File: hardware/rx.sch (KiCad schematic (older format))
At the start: 19 parts, among them P1 SMA, U11 SKY65404, U9 TRF37A73

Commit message: Current working version.
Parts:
- C179, C180, C42, C44, C46, C48, C49: footprint fmcw3:C_0402b -> Capacitor_SMD:C_0402_1005Metric; symbol C -> Device:C
- C35, C47, C50, C54: footprint fmcw3:C_0603b -> Capacitor_SMD:C_0603_1608Metric; symbol C -> Device:C
- FB7, FB8: symbol FILTER -> Device:Ferrite_Bead
- L1, L2: symbol INDUCTOR -> Device:L
- P1: symbol SMA -> fmcw3-rescue:SMA
- R22: symbol R -> Device:R
- U11: symbol SKY65404 -> fmcw3-rescue:SKY65404
- U9: symbol TRF37A75 -> fmcw3-rescue:TRF37A75
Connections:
- wire segments 39 -> 54

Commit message: Dropped the 3 from the end of the project name.
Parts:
- FB7, FB8: footprint fmcw3:C_0603b -> fmcw:C_0603b
- L1, L2: footprint fmcw3:C_0402b -> fmcw:C_0402b
- P1: footprint fmcw3:CONSMA003.062 -> fmcw:CONSMA003.062; symbol fmcw3-rescue:SMA -> fmcw-rescue:SMA-fmcw3-rescue
- R22: footprint fmcw3:R_0402b -> fmcw:R_0402b
- U11: footprint fmcw3:XFDFN-6 -> fmcw:XFDFN-6; symbol fmcw3-rescue:SKY65404 -> fmcw-rescue:SKY65404-fmcw3-rescue
- U9: footprint fmcw3:DFN-8-1EP_2x2mm_Pitch0.5mm -> fmcw:DFN-8-1EP_2x2mm_Pitch0.5mm; symbol fmcw3-rescue:TRF37A75 -> fmcw-rescue:TRF37A75-fmcw3-rescue

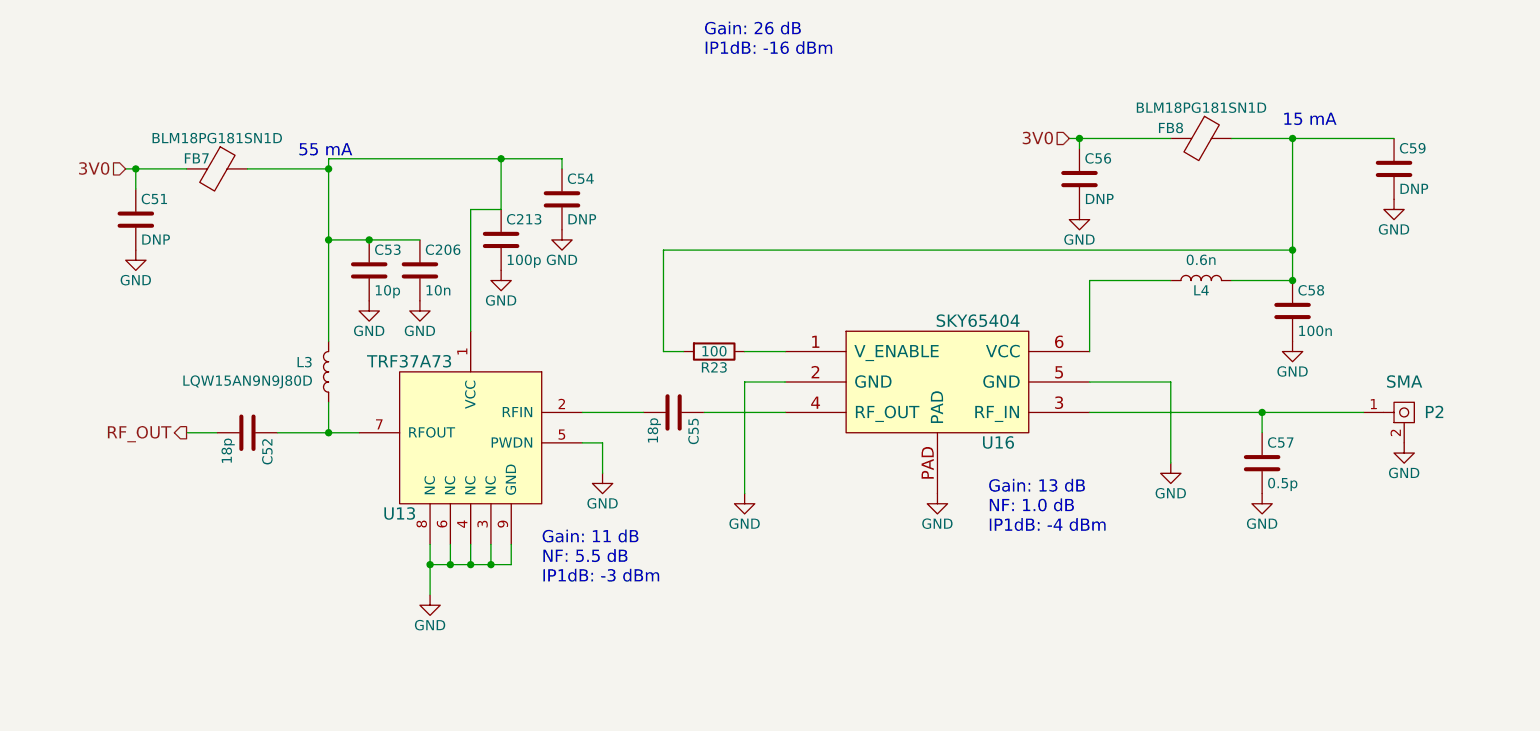
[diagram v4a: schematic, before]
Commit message: Improved top level documentation.
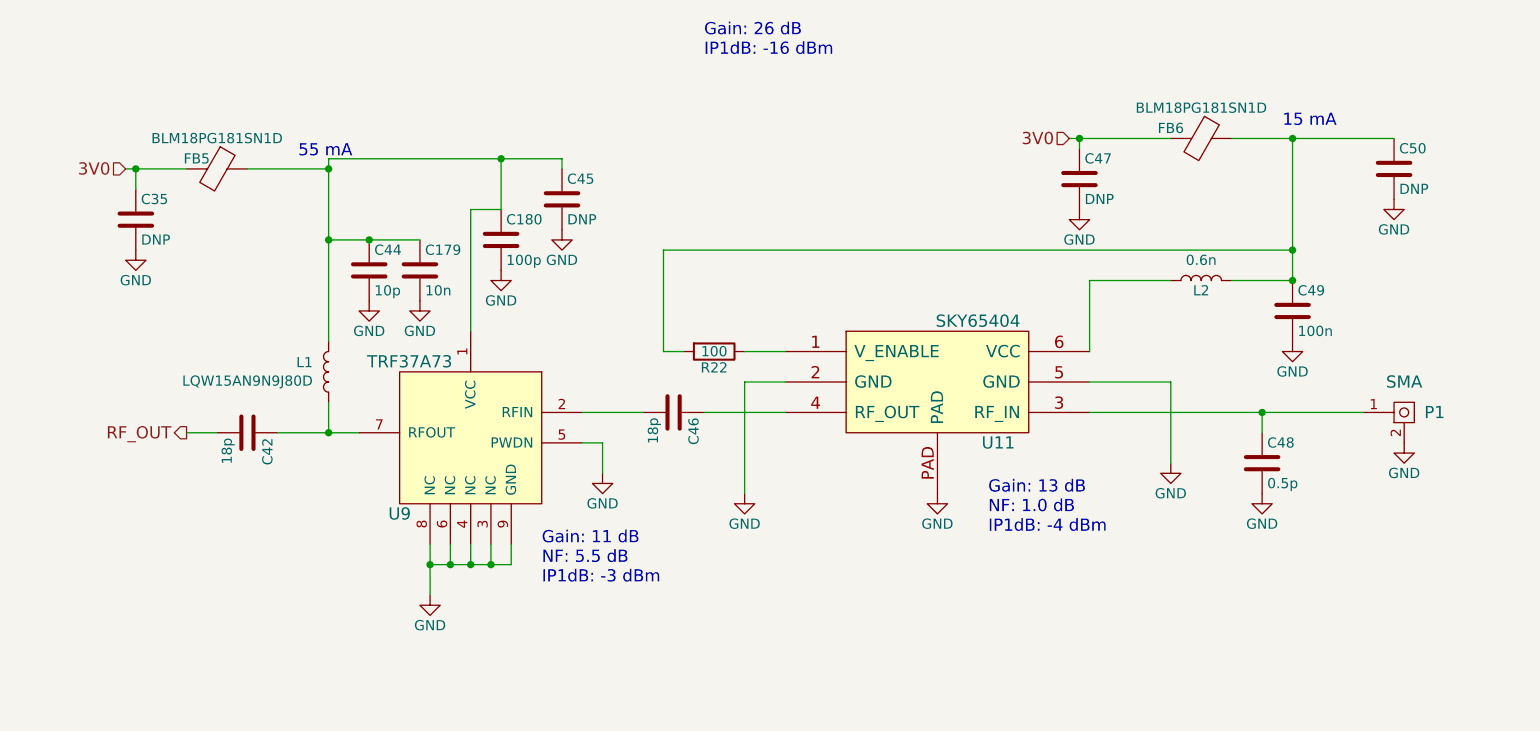
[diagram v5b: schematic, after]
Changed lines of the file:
@@
 $Descr A4 11693 8268
 encoding utf-8
-Sheet 7 10
+Sheet 6 10
 Title ""
 Date ""
@@
 AR Path="/59396B97/593BC199" Ref="U11"  Part="1"
 AR Path="/593D90BA/593BC199" Ref="U16"  Part="1"
-F 0 "U16" H 7150 3500 60  0000 C CNN
+F 0 "U11" H 7150 3500 60  0000 C CNN
 F 1 "SKY65404" H 7050 4100 60  0000 C CNN
 F 2 "fmcw:XFDFN-6" H 6750 3800 60  0001 C CNN
@@
 AR Path="/59396B97/593BC25F" Ref="#PWR0124"  Part="1"
 AR Path="/593D90BA/593BC25F" Ref="#PWR0139"  Part="1"
-F 0 "#PWR0139" H 6850 4100 50  0001 C CNN
+F 0 "#PWR0124" H 6850 4100 50  0001 C CNN
 F 1 "GND" H 6850 4200 50  0000 C CNN
 F 2 "" H 6850 4350 60  0000 C CNN
@@
 AR Path="/59396B97/593BC2B3" Ref="#PWR0125"  Part="1"
 AR Path="/593D90BA/593BC2B3" Ref="#PWR0140"  Part="1"
-F 0 "#PWR0140" H 8000 3950 50  0001 C CNN
+F 0 "#PWR0125" H 8000 3950 50  0001 C CNN
 F 1 "GND" H 8000 4050 50  0000 C CNN
 F 2 "" H 8000 4200 60  0000 C CNN
@@
 AR Path="/59396B97/593BC302" Ref="#PWR0126"  Part="1"
 AR Path="/593D90BA/593BC302" Ref="#PWR0141"  Part="1"
-F 0 "#PWR0141" H 5900 4100 50  0001 C CNN
+F 0 "#PWR0126" H 5900 4100 50  0001 C CNN
 F 1 "GND" H 5900 4200 50  0000 C CNN
 F 2 "" H 5900 4350 60  0000 C CNN
@@
 AR Path="/59396B97/593BC396" Ref="R22"  Part="1"
 AR Path="/593D90BA/593BC396" Ref="R23"  Part="1"
-F 0 "R23" V 5830 3650 50  0000 C CNN
+F 0 "R22" V 5830 3650 50  0000 C CNN
 F 1 "100" V 5750 3650 50  0000 C CNN
 F 2 "fmcw:R_0402b" V 5680 3650 30  0001 C CNN
@@
 AR Path="/59396B97/593BC695" Ref="L2"  Part="1"
 AR Path="/593D90BA/593BC695" Ref="L4"  Part="1"
-F 0 "L4" V 8100 3300 50  0000 C CNN
+F 0 "L2" V 8100 3300 50  0000 C CNN
 F 1 "0.6n" V 8250 3300 50  0000 C CNN
 F 2 "fmcw:C_0402b" H 8150 3300 60  0001 C CNN
@@
 AR Path="/59396B97/593BC767" Ref="C49"  Part="1"
 AR Path="/593D90BA/593BC767" Ref="C58"  Part="1"
-F 0 "C58" H 8625 3550 50  0000 L CNN
+F 0 "C49" H 8625 3550 50  0000 L CNN
 F 1 "100n" H 8625 3350 50  0000 L CNN
 F 2 "Capacitor_SMD:C_0402_1005Metric" H 8638 3300 30  0001 C CNN
@@
 AR Path="/59396B97/593BC7DB" Ref="#PWR0127"  Part="1"
 AR Path="/593D90BA/593BC7DB" Ref="#PWR0142"  Part="1"
-F 0 "#PWR0142" H 8600 3350 50  0001 C CNN
+F 0 "#PWR0127" H 8600 3350 50  0001 C CNN
 F 1 "GND" H 8600 3450 50  0000 C CNN
 F 2 "" H 8600 3600 60  0000 C CNN
@@
 AR Path="/59396B97/593BCCCA" Ref="P1"  Part="1"
 AR Path="/593D90BA/593BCCCA" Ref="P2"  Part="1"
-F 0 "P2" H 9300 3950 60  0000 C CNN
+F 0 "P1" H 9300 3950 60  0000 C CNN
 F 1 "SMA" H 9150 4100 60  0000 C CNN
 F 2 "fmcw:CONSMA003.062" H 9150 3950 60  0001 C CNN
@@
 AR Path="/59396B97/593BCD59" Ref="#PWR0128"  Part="1"
 AR Path="/593D90BA/593BCD59" Ref="#PWR0143"  Part="1"
-F 0 "#PWR0143" H 9150 3850 50  0001 C CNN
+F 0 "#PWR0128" H 9150 3850 50  0001 C CNN
 F 1 "GND" H 9150 3950 50  0000 C CNN
 F 2 "" H 9150 4100 60  0000 C CNN
@@
 AR Path="/59396B97/593BCEBC" Ref="C48"  Part="1"
 AR Path="/593D90BA/593BCEBC" Ref="C57"  Part="1"
-F 0 "C57" H 8475 4300 50  0000 L CNN
+F 0 "C48" H 8475 4300 50  0000 L CNN
 F 1 "0.5p" H 8475 4100 50  0000 L CNN
 F 2 "Capacitor_SMD:C_0402_1005Metric" H 8488 4050 30  0001 C CNN
@@
 AR Path="/59396B97/593BCF37" Ref="#PWR0129"  Part="1"
 AR Path="/593D90BA/593BCF37" Ref="#PWR0144"  Part="1"
-F 0 "#PWR0144" H 8450 4100 50  0001 C CNN
+F 0 "#PWR0129" H 8450 4100 50  0001 C CNN
 F 1 "GND" H 8450 4200 50  0000 C CNN
 F 2 "" H 8450 4350 60  0000 C CNN
@@
 AR Path="/59396B97/593BD4EF" Ref="C46"  Part="1"
 AR Path="/593D90BA/593BD4EF" Ref="C55"  Part="1"
-F 0 "C55" H 5575 4050 50  0000 L CNN
+F 0 "C46" H 5575 4050 50  0000 L CNN
 F 1 "18p" H 5575 3850 50  0000 L CNN
 F 2 "Capacitor_SMD:C_0402_1005Metric" H 5588 3800 30  0001 C CNN
@@
 AR Path="/59396B97/593BD727" Ref="#PWR0130"  Part="1"
 AR Path="/593D90BA/593BD727" Ref="#PWR0145"  Part="1"
-F 0 "#PWR0145" H 4350 4600 50  0001 C CNN
+F 0 "#PWR0130" H 4350 4600 50  0001 C CNN
 F 1 "GND" H 4350 4700 50  0000 C CNN
 F 2 "" H 4350 4850 60  0000 C CNN
@@
 AR Path="/59396B97/593BD8E8" Ref="L1"  Part="1"
 AR Path="/593D90BA/593BD8E8" Ref="L3"  Part="1"
-F 0 "L3" H 3928 3704 50  0000 L CNN
+F 0 "L1" H 3928 3704 50  0000 L CNN
 F 1 "LQW15AN9N9J80D" H 3928 3795 50  0000 L CNN
 F 2 "fmcw:C_0402b" H 3850 3750 60  0001 C CNN
@@
 AR Path="/59396B97/593BDA25" Ref="C44"  Part="1"
 AR Path="/593D90BA/593BDA25" Ref="C53"  Part="1"
-F 0 "C53" H 4075 3350 50  0000 L CNN
+F 0 "C44" H 4075 3350 50  0000 L CNN
 F 1 "10p" H 4075 3150 50  0000 L CNN
 F 2 "Capacitor_SMD:C_0402_1005Metric" H 4088 3100 30  0001 C CNN
@@
 AR Path="/59396B97/593BDABD" Ref="#PWR0131"  Part="1"
 AR Path="/593D90BA/593BDABD" Ref="#PWR0146"  Part="1"
-F 0 "#PWR0146" H 4050 3150 50  0001 C CNN
+F 0 "#PWR0131" H 4050 3150 50  0001 C CNN
 F 1 "GND" H 4050 3250 50  0000 C CNN
 F 2 "" H 4050 3400 60  0000 C CNN
@@
 AR Path="/59396B97/593BDF98" Ref="C42"  Part="1"
 AR Path="/593D90BA/593BDF98" Ref="C52"  Part="1"
-F 0 "C52" H 3475 4150 50  0000 L CNN
+F 0 "C42" H 3475 4150 50  0000 L CNN
 F 1 "18p" H 3475 3950 50  0000 L CNN
 F 2 "Capacitor_SMD:C_0402_1005Metric" H 3488 3900 30  0001 C CNN
@@
 AR Path="/593D90BA/59751767" Ref="FB7"  Part="1"
 AR Path="/59396B97/59751767" Ref="FB5"  Part="1"
-F 0 "FB7" V 3250 2650 50  0000 C CNN
+F 0 "FB5" V 3250 2650 50  0000 C CNN
 F 1 "BLM18PG181SN1D" V 3150 2750 50  0000 C CNN
 F 2 "fmcw:C_0603b" H 3300 2750 60  0001 C CNN
@@
 AR Path="/593D90BA/59751D28" Ref="C54"  Part="1"
 AR Path="/59396B97/59751D28" Ref="C45"  Part="1"
-F 0 "C54" H 5025 3000 50  0000 L CNN
+F 0 "C45" H 5025 3000 50  0000 L CNN
 F 1 "DNP" H 5025 2800 50  0000 L CNN
 F 2 "Capacitor_SMD:C_0603_1608Metric" H 5038 2750 30  0001 C CNN
@@
 AR Path="/593D90BA/59751D9B" Ref="#PWR0147"  Part="1"
 AR Path="/59396B97/59751D9B" Ref="#PWR0132"  Part="1"
-F 0 "#PWR0147" H 5000 2800 50  0001 C CNN
+F 0 "#PWR0132" H 5000 2800 50  0001 C CNN
 F 1 "GND" H 5000 2900 50  0000 C CNN
 F 2 "" H 5000 3050 60  0000 C CNN
@@
 AR Path="/59396B97/59752286" Ref="C35"  Part="1"
 AR Path="/593D90BA/59752286" Ref="C51"  Part="1"
-F 0 "C51" H 2925 3100 50  0000 L CNN
+F 0 "C35" H 2925 3100 50  0000 L CNN
 F 1 "DNP" H 2925 2900 50  0000 L CNN
 F 2 "Capacitor_SMD:C_0603_1608Metric" H 2938 2850 30  0001 C CNN
@@
 AR Path="/593D90BA/59752325" Ref="#PWR0148"  Part="1"
 AR Path="/59396B97/59752325" Ref="#PWR0133"  Part="1"
-F 0 "#PWR0148" H 2900 2900 50  0001 C CNN
+F 0 "#PWR0133" H 2900 2900 50  0001 C CNN
 F 1 "GND" H 2900 3000 50  0000 C CNN
 F 2 "" H 2900 3150 60  0000 C CNN
@@
 AR Path="/593D90BA/597527FA" Ref="FB8"  Part="1"
 AR Path="/59396B97/597527FA" Ref="FB6"  Part="1"
-F 0 "FB8" V 8100 2450 50  0000 C CNN
+F 0 "FB6" V 8100 2450 50  0000 C CNN
 F 1 "BLM18PG181SN1D" V 8000 2600 50  0000 C CNN
 F 2 "fmcw:C_0603b" H 8150 2600 60  0001 C CNN
@@
 AR Path="/59396B97/59752C43" Ref="C50"  Part="1"
 AR Path="/593D90BA/59752C43" Ref="C59"  Part="1"
-F 0 "C59" H 9125 2850 50  0000 L CNN
+F 0 "C50" H 9125 2850 50  0000 L CNN
 F 1 "DNP" H 9125 2650 50  0000 L CNN
 F 2 "Capacitor_SMD:C_0603_1608Metric" H 9138 2600 30  0001 C CNN
@@
 AR Path="/59396B97/59752C49" Ref="#PWR0134"  Part="1"
 AR Path="/593D90BA/59752C49" Ref="#PWR0149"  Part="1"
-F 0 "#PWR0149" H 9100 2650 50  0001 C CNN
+F 0 "#PWR0134" H 9100 2650 50  0001 C CNN
 F 1 "GND" H 9100 2750 50  0000 C CNN
 F 2 "" H 9100 2900 60  0000 C CNN
@@
 AR Path="/59396B97/59752CDE" Ref="C47"  Part="1"
 AR Path="/593D90BA/59752CDE" Ref="C56"  Part="1"
-F 0 "C56" H 7575 2900 50  0000 L CNN
+F 0 "C47" H 7575 2900 50  0000 L CNN
 F 1 "DNP" H 7575 2700 50  0000 L CNN
 F 2 "Capacitor_SMD:C_0603_1608Metric" H 7588 2650 30  0001 C CNN
@@
 AR Path="/59396B97/59752CE4" Ref="#PWR0135"  Part="1"
 AR Path="/593D90BA/59752CE4" Ref="#PWR0150"  Part="1"
-F 0 "#PWR0150" H 7550 2700 50  0001 C CNN
+F 0 "#PWR0135" H 7550 2700 50  0001 C CNN
 F 1 "GND" H 7550 2800 50  0000 C CNN
 F 2 "" H 7550 2950 60  0000 C CNN
@@
 AR Path="/593D90BA/597605DF" Ref="U13"  Part="1"
 AR Path="/597605DF" Ref="U13"  Part="1"
-F 0 "U13" H 4900 3750 60  0000 C CNN
+F 0 "U9" H 4900 3750 60  0000 C CNN
 F 1 "TRF37A73" H 4850 4500 60  0000 C CNN
 F 2 "fmcw:DFN-8-1EP_2x2mm_Pitch0.5mm" H 4350 4050 60  0001 C CNN
@@
 AR Path="/59396B97/59761DBE" Ref="C180"  Part="1"
 AR Path="/593D90BA/59761DBE" Ref="C213"  Part="1"
-F 0 "C213" H 4725 3200 50  0000 L CNN
+F 0 "C180" H 4725 3200 50  0000 L CNN
 F 1 "100p" H 4725 3000 50  0000 L CNN
 F 2 "Capacitor_SMD:C_0402_1005Metric" H 4738 2950 30  0001 C CNN
@@
 AR Path="/59396B97/59761E7D" Ref="#PWR0136"  Part="1"
 AR Path="/593D90BA/59761E7D" Ref="#PWR0151"  Part="1"
-F 0 "#PWR0151" H 4700 3000 50  0001 C CNN
+F 0 "#PWR0136" H 4700 3000 50  0001 C CNN
 F 1 "GND" H 4700 3100 50  0000 C CNN
 F 2 "" H 4700 3250 60  0000 C CNN
@@
 AR Path="/59396B97/59762FC5" Ref="C179"  Part="1"
 AR Path="/593D90BA/59762FC5" Ref="C206"  Part="1"
-F 0 "C206" H 4325 3350 50  0000 L CNN
+F 0 "C179" H 4325 3350 50  0000 L CNN
 F 1 "10n" H 4325 3150 50  0000 L CNN
 F 2 "Capacitor_SMD:C_0402_1005Metric" H 4338 3100 30  0001 C CNN
@@
 AR Path="/59396B97/5976305E" Ref="#PWR0137"  Part="1"
 AR Path="/593D90BA/5976305E" Ref="#PWR0152"  Part="1"
-F 0 "#PWR0152" H 4300 3150 50  0001 C CNN
+F 0 "#PWR0137" H 4300 3150 50  0001 C CNN
 F 1 "GND" H 4300 3250 50  0000 C CNN
 F 2 "" H 4300 3400 60  0000 C CNN
@@
 AR Path="/593D90BA/59765731" Ref="#PWR0153"  Part="1"
 AR Path="/59396B97/59765731" Ref="#PWR0138"  Part="1"
-F 0 "#PWR0153" H 5200 4000 50  0001 C CNN
+F 0 "#PWR0138" H 5200 4000 50  0001 C CNN
 F 1 "GND" H 5200 4100 50  0000 C CNN
 F 2 "" H 5200 4250 60  0000 C CNN
